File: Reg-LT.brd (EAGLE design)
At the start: 94 x 71.6 mm, 64 parts, among them IC1 MEGA8-AI, IC2 DS1813-SMD, IC3 LM1117IMPX-3.3, IC4 LM321MF, IC5 LM321MF, Q1 20 MHz, X1 22-23-2021, X2 MKDSN1,5/3-5,08, X3 MKDSN1,5/3-5,08, X4 MKDSN1,5/3-5,08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

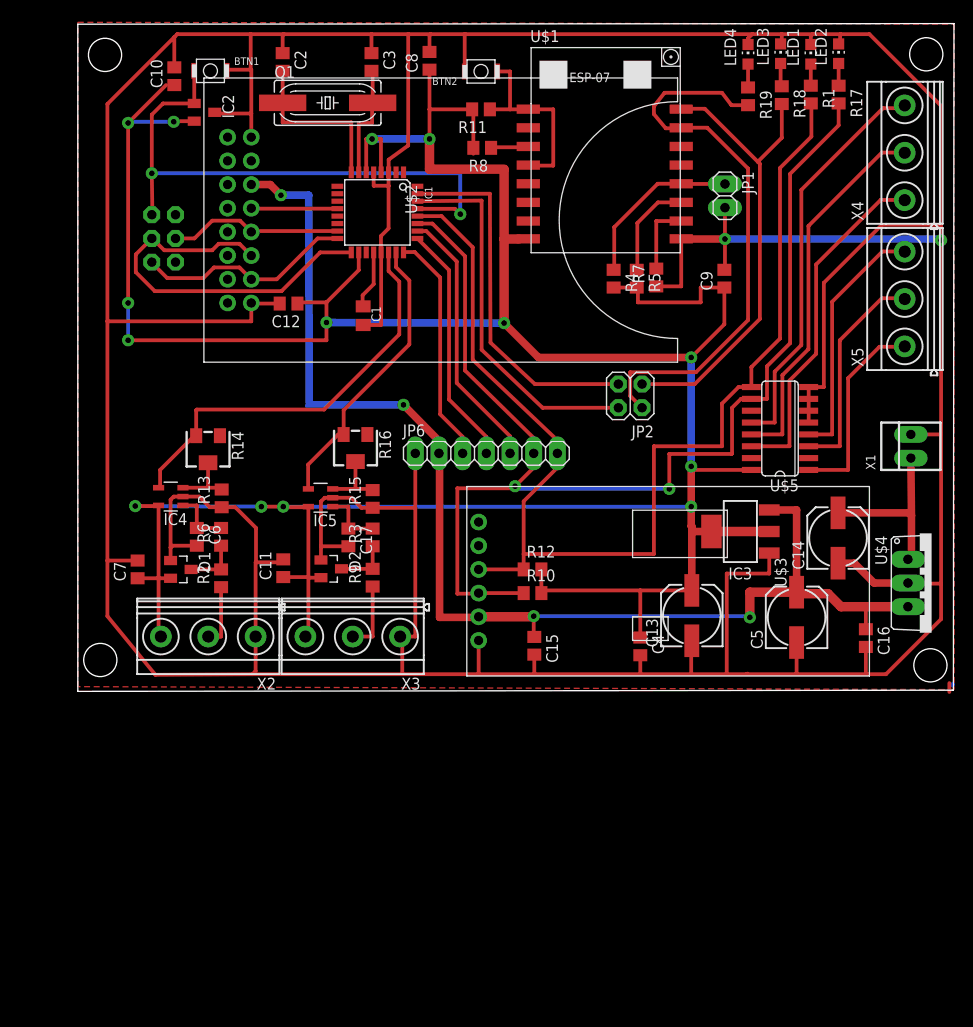
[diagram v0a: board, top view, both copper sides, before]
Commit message: sd-card no-module
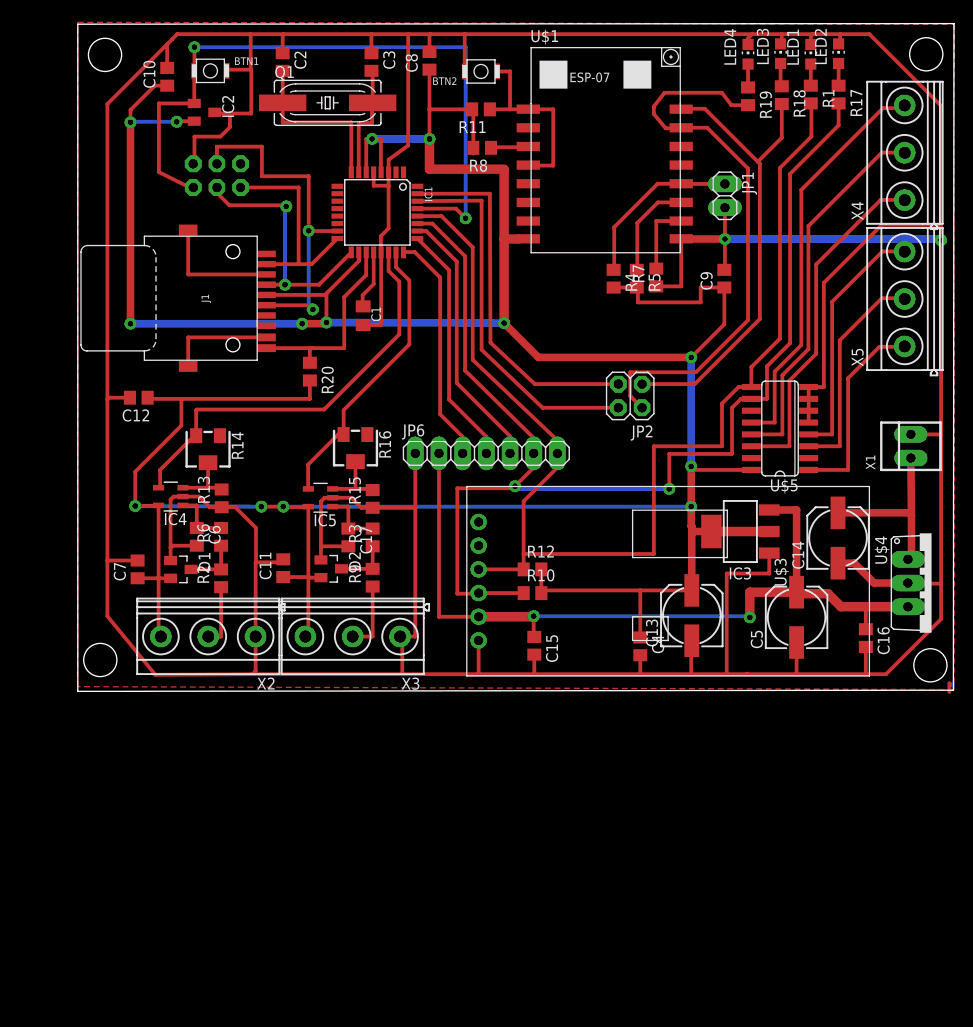
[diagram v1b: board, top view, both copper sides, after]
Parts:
- removed U$2: SD-CARDSD-MODULE2X8-H, MyLib:SD_MODULE-2X8H
- added J1: ATTEND-MICROSD-112, MyLib:ATTEND-112
- added R20: 10k, rcl:R0805
- moved C12 19.0 mm to (3.24, 31.6)
- moved JP4 8.83 mm to (11.6, 55.4), turned to 0 degrees
- moved C10 0.76 mm to (6.29, 66.0)
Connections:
- new net SD_DETECT: IC1.19, J1.CD, R20.1
- net +3V3: now also J1.VDD, R20.2; no longer U$2.+3V3
- net +5V: no longer U$2.+5V
- net CS_SD: no longer U$2.CS
- net GND: now also J1.GND, J1.S1, J1.S2, J1.VSS; no longer U$2.GND@1, U$2.GND@2
- net MISO: now also J1.DAT0; no longer U$2.MISO
- net MOSI: now also J1.CMD; no longer U$2.MOSI
- net SCK: now also J1.CLK; no longer U$2.SCK
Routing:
- net +5V: track 134.0 -> 87.7 mm, vias 4 -> 2
- net +3V3: track 364.0 -> 397.2 mm
- net SD_DETECT: track 0.00 -> 21.1 mm
- net MOSI: track 18.7 -> 38.1 mm, vias 0 -> 2
- net SCK: track 42.0 -> 27.7 mm, vias 0 -> 2
- net RESET: track 61.7 -> 74.3 mm
- net GND: track 607.8 -> 619.9 mm
- net CS_SD: track 9.31 -> 0.06 mm

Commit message: timer - no-module
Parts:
- removed C15, C16: 0.1, rcl:C0805
- removed JP6: (no value), pinhead:1X07
- removed LED1, LED2, LED3, LED4: (no value), led:CHIP-LED0805
- removed R18, R19: 1k, rcl:R0805
- removed U$3: RTCRTC_MODULE-1X6H, MyLib:RTC_MODULE-1X6H
- removed U$4: LM7805TO-220-VERT, MyLib:TO220AV
- added D3: BAT54S, diode:SOT23
- added D4: 1N4004, diode:DO41-10
- added G1: CR2032H, MyLib:CR2032H
- added IC7: PCF8583T, MyLib:SO8-7_5
- added JP3: (no value), pinhead:1X06
- added Q2: (no value), MyLib:MA306
- added X6: MKDSN1,5/3-5,08, con-phoenix-508:MKDSN1,5/3-5,08
- C5: value (none) -> 0.1; device rcl:153CLV-0605 -> rcl:C0805
- R1, R17: value 1k -> 100
- moved R17 129.8 mm to (-7.62, -33.2), turned to 0 degrees
- moved R1 112.6 mm to (-0.44, -19.2), turned to 0 degrees
- moved X4 26.4 mm to (85.6, 34.0)
- moved X5 26.1 mm to (85.6, 18.6)
- moved X1 23.2 mm to (73.5, 6.86), turned to 0 degrees
- moved C9 20.7 mm to (45.3, 44.0), turned to 270 degrees
- moved C12 20.3 mm to (5.33, 51.8), turned to 0 degrees
- moved R10 18.8 mm to (58.9, 23.7)
- moved C14 16.8 mm to (64.5, 6.99)
- moved R12 15.9 mm to (59.0, 21.5)
- moved C5 14.9 mm to (67.9, 21.7), turned to 270 degrees
- moved C13 13.3 mm to (49.3, 6.86)
- moved IC3 11.7 mm to (57.0, 12.7), turned to 0 degrees
- moved JP2 7.26 mm to (49.7, 35.5)
- moved U$5 6.09 mm to (75.1, 23.0), turned to 0 degrees
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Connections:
- removed net +5V: C15.1, C16.1, C5.+, IC3.3, JP6.2, U$3.VCC, U$4.VOUT
- removed net N$32: LED4.A, R19.1
- new net N$15: IC7.1, Q2.1
- new net N$16: IC7.2, Q2.4
- new net N$33: G1.+, IC7.3
- net +3V3: now also C5.1, D3.2, IC7.8, X6.3
- net GND: now also C5.2, D3.1, G1.-, IC7.4, JP3.1, R17.1, X6.1; no longer C15.2, C16.2, C5.-, JP6.1, LED1.C, LED2.C, LED3.C, LED4.C, U$3.GND, U$4.GND
- net N$29: now also D3.3, R1.2; no longer LED1.A, R1.1
- net N$30: now also R1.1, X6.2; no longer LED2.A, R17.1
- net N$31: now also R17.2; no longer LED3.A, R18.1
- net PC1: now also JP3.2; no longer JP6.3
- net PC2: now also JP3.3; no longer JP6.4
- net PC3: now also JP3.4; no longer JP6.5
- net PW: now also IC3.3; no longer U$4.VIN
- net RX_ESP: no longer R19.2
- net SCL: now also IC7.6, JP3.6; no longer JP6.7, R1.2, U$3.SCL
- net SDA: now also IC7.5, JP3.5; no longer JP6.6, R17.2, U$3.SDA
- net TX_ESP: no longer R18.2
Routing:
- net +5V: track 87.7 -> 0.00 mm, vias 2 -> 0
- net SDA: track 131.1 -> 75.7 mm, vias 2 -> 0
- net +3V3: track 397.2 -> 360.1 mm, vias 14 -> 16
- net SCL: track 126.6 -> 92.6 mm, vias 0 -> 2
- net GND: track 619.9 -> 592.1 mm, vias 2 -> 0
- net RX_ESP: track 60.5 -> 33.2 mm
- net N$23: track 43.7 -> 24.0 mm
- net N$25: track 37.2 -> 17.8 mm
- net N$18: track 40.5 -> 21.1 mm
- net TX_ESP: track 50.3 -> 32.1 mm
- net N$28: track 26.8 -> 14.3 mm
- net TXD: track 39.2 -> 29.0 mm
- net RXD: track 40.0 -> 30.0 mm
- net N$27: track 23.6 -> 15.0 mm
- net N$33: track 0.00 -> 5.95 mm
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
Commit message: no amplifires
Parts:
- removed C17, C6: 10,0, rcl:C0805
- removed D3: BAT54S, diode:SOT23
- removed D4: 1N4004, diode:DO41-10
- removed IC4, IC5: LM321MF, linear:SOT23-5
- removed R1, R17: 100, rcl:R0805
- removed R13, R15: 10k, rcl:R0805
- removed R14, R16: 10k, rcl:RTRIM3214W
- removed X2, X3: MKDSN1,5/3-5,08, con-phoenix-508:MKDSN1,5/3-5,08
- added D5, D6: 1N4148DO35-7, diode:DO35-7
- added X7: MKDSN1,5/2-5,08, con-phoenix-508:MKDSN1,5/2-5,08
- D1, D2: value BAT54S -> BAV199
- R2, R9: value 100 -> (none); device rcl:R0805 -> rcl:VMTA55
- R3, R6: value 1.5k -> (none); device rcl:R0805 -> rcl:VMTA55
- X6: value MKDSN1,5/3-5,08 -> MKDSN1,5/2-5,08; device con-phoenix-508:MKDSN1,5/3-5,08 -> con-phoenix-508:MKDSN1,5/2-5,08
- moved R9 27.8 mm to (0.76, 15.7), turned to 270 degrees
- moved X6 24.6 mm to (19.1, 4.89)
- moved C7 20.4 mm to (23.4, 11.2), turned to 270 degrees
- moved R3 17.0 mm to (11.4, 15.9)
- moved D2 16.8 mm to (7.37, 16.1), turned to 0 degrees
- moved C9 16.1 mm to (61.4, 44.5), turned to 90 degrees
- moved D1 15.0 mm to (22.4, 16.4), turned to 0 degrees
- moved R2 14.8 mm to (26.4, 16.1)
- moved C11 10.6 mm to (8.32, 11.4), turned to 270 degrees
- moved R7 9.71 mm to (66.3, 50.5), turned to 180 degrees
- moved R6 3.79 mm to (15.7, 15.7), turned to 270 degrees
- moved R4 2.42 mm to (56.6, 44.5)
- moved R5 2.29 mm to (58.9, 44.5)
- moved JP1 1.37 mm to (66.6, 54.5), turned to 0 degrees
- moved C8 0.13 mm to (34.4, 67.6)
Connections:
- removed net N$13: D2.3, R3.1, R9.2
- removed net N$17: IC5.3, R15.2, R16.2
- removed net N$29: D3.3, R1.2
- removed net N$30: R1.1, X6.2
- removed net N$31: R17.2
- removed net N$70: C6.1, IC4.1, R6.2
- removed net N$8: C17.1, IC5.1, R3.2
- removed net RESET_ESP: BTN2.1, R11.1, U$1.GPIO16, U$1.REST
- net +3V3: no longer D3.2, IC4.5, IC5.5, X2.3, X3.3, X6.3
- net GND: now also R6.1, R9.1, X7.1; no longer C17.2, C6.2, D3.1, IC4.2, IC5.2, R13.1, R15.1, R17.1, X2.1, X3.1
- net N$1: now also D5.A; no longer R6.1
- net N$14: now also R2.1, X6.2; no longer R9.1, X3.2
- net N$24: now also D5.C, R6.2; no longer IC5.4, R16.3
- net N$5: now also R3.1, X7.2; no longer R2.1, X2.2
- net N$6: now also D2.3, D6.A, R3.2; no longer IC4.3, R13.2, R14.2
- net N$7: now also D6.C, R9.2; no longer IC4.4, R14.3
- net T0: now also BTN2.1, R11.1, U$1.GPIO16, U$1.REST
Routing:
- net GND: track 592.1 -> 107.8 mm
- net T0: track 0.00 -> 71.9 mm
- net +3V3: track 360.1 -> 331.0 mm
- net RESET_ESP: track 21.0 -> 0.00 mm
- net N$24: track 30.8 -> 47.2 mm
- net N$7: track 44.5 -> 60.8 mm
- net N$17: track 7.46 -> 0.00 mm
- net N$1: track 5.77 -> 12.9 mm
- net N$8: track 6.64 -> 0.00 mm
- net N$70: track 6.51 -> 0.00 mm
- net N$6: track 7.04 -> 12.9 mm
- net N$13: track 5.77 -> 0.00 mm
- net N$11: track 7.81 -> 4.00 mm
- net N$9: track 18.8 -> 16.3 mm
- net N$10: track 10.7 -> 9.16 mm
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
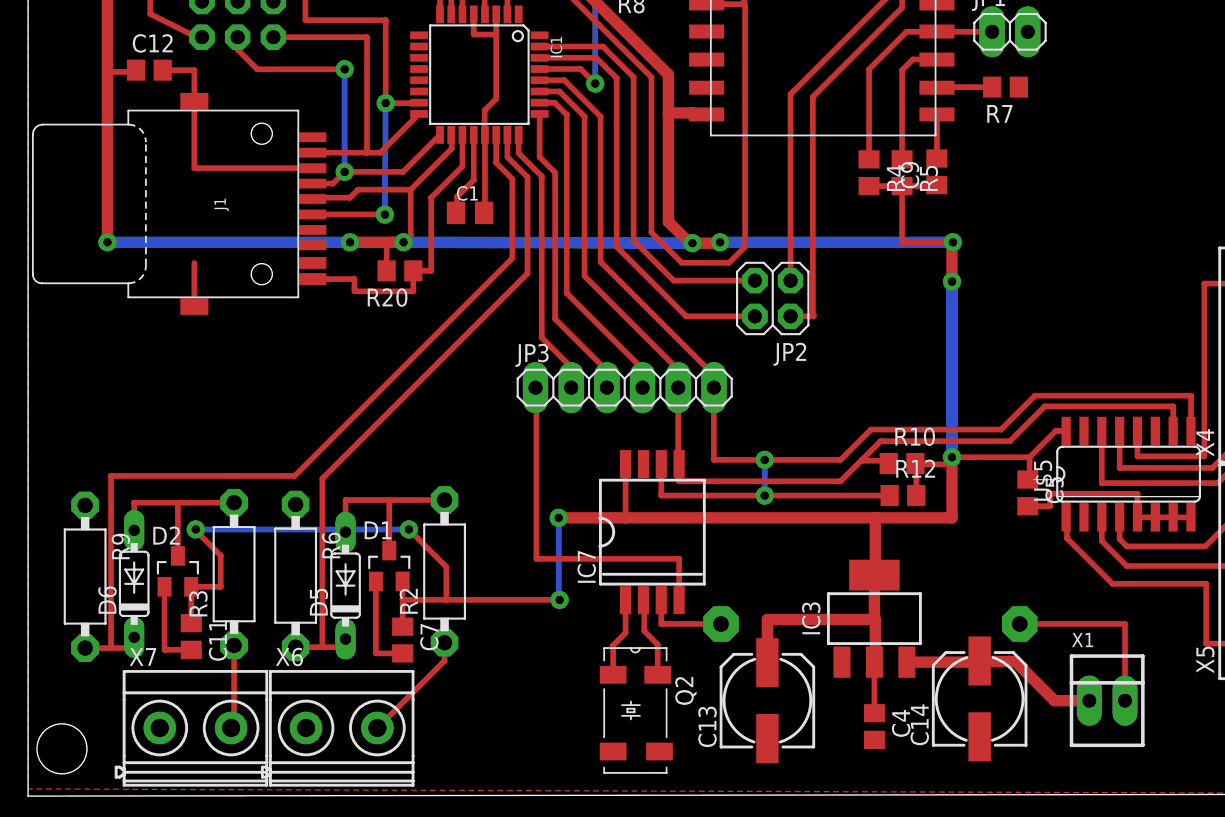
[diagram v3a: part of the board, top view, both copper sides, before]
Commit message: input-rectifier
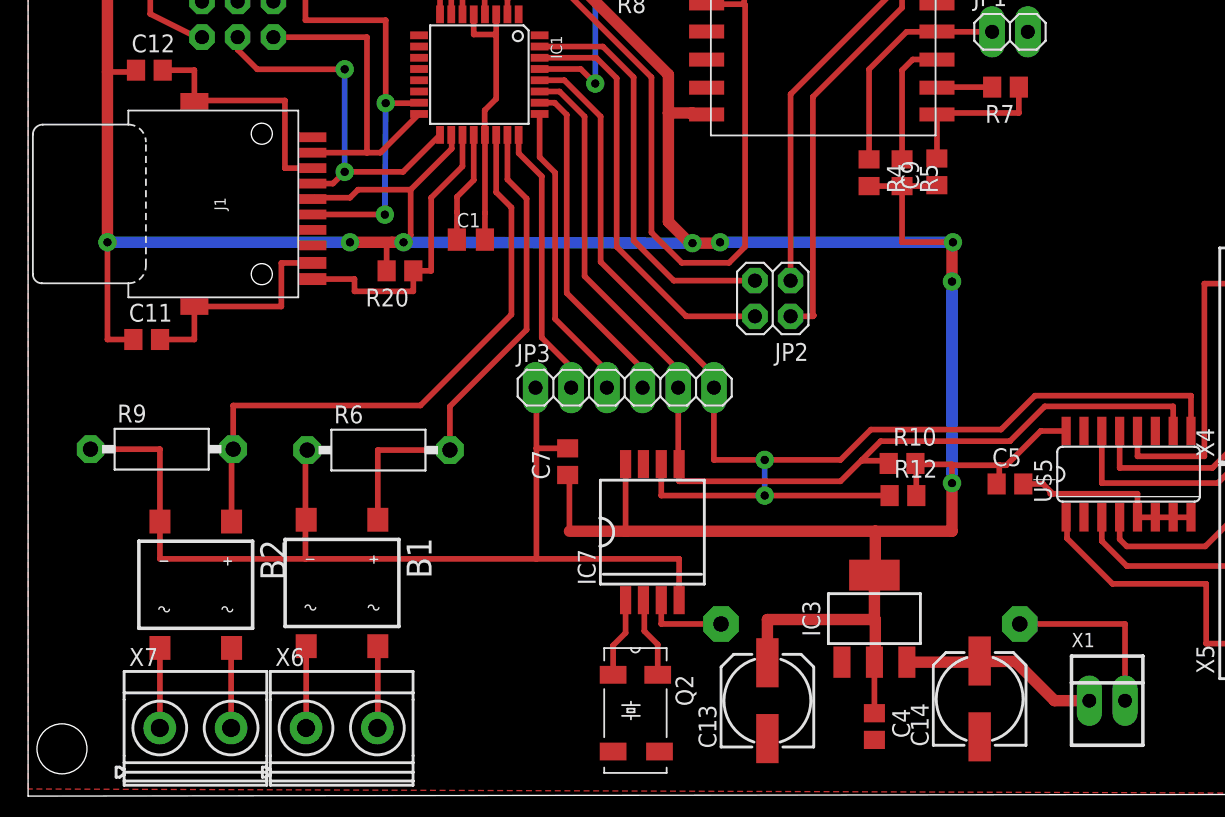
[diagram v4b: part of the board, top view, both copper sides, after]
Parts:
- removed D1, D2: BAV199, diode:SOT23
- removed D5, D6: 1N4148DO35-7, diode:DO35-7
- removed R2, R3: (no value), rcl:VMTA55
- added B1, B2: DF08S, rectifier:DFS
- moved C11 21.4 mm to (5.14, 32.6), turned to 0 degrees
- moved C7 17.3 mm to (35.1, 23.9), turned to 90 degrees
- moved R6 10.7 mm to (21.7, 24.7), turned to 0 degrees
- moved R9 10.6 mm to (6.22, 24.8), turned to 0 degrees
- moved C1 1.91 mm to (28.2, 39.7)
- moved C5 1.42 mm to (66.6, 22.3), turned to 0 degrees
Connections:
- removed net N$14: R2.1, X6.2
- removed net N$6: D2.3, D6.A, R3.2
- new net N$13: B1.AC1, X6.2
- new net N$8: B1.AC2, X6.1
- net +3V3: no longer D1.2, D2.2
- net GND: now also B1.-, B2.-; no longer D1.1, D2.1, X6.1, X7.1
- net N$1: now also B2.AC1, X7.2; no longer D1.3, D5.A, R2.2
- net N$24: now also B1.+; no longer D5.C
- net N$5: now also B2.AC2, X7.1; no longer R3.1, X7.2
- net N$7: now also B2.+; no longer D6.C
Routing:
- net GND: track 107.8 -> 166.6 mm
- net +3V3: track 331.0 -> 293.8 mm, vias 16 -> 12
- net N$7: track 60.8 -> 44.1 mm
- net N$6: track 12.9 -> 0.00 mm
- net N$24: track 47.2 -> 35.4 mm
- net N$14: track 8.05 -> 0.00 mm
- net N$1: track 12.9 -> 5.73 mm
- net N$13: track 0.00 -> 5.86 mm
- net N$8: track 0.00 -> 5.84 mm
- net N$2: track 6.11 -> 7.98 mm
